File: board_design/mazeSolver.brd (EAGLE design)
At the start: 130 x 130 mm, 53 parts, among them IC1 L293DD, IC2 7805TV, IC3 CP2101, Q1 BC547, Q2 BC547, U1 MPU-9250, U2 AP1509-SOP8L, U3 ESP-WROOM-32, U4 GY-521MPU6050

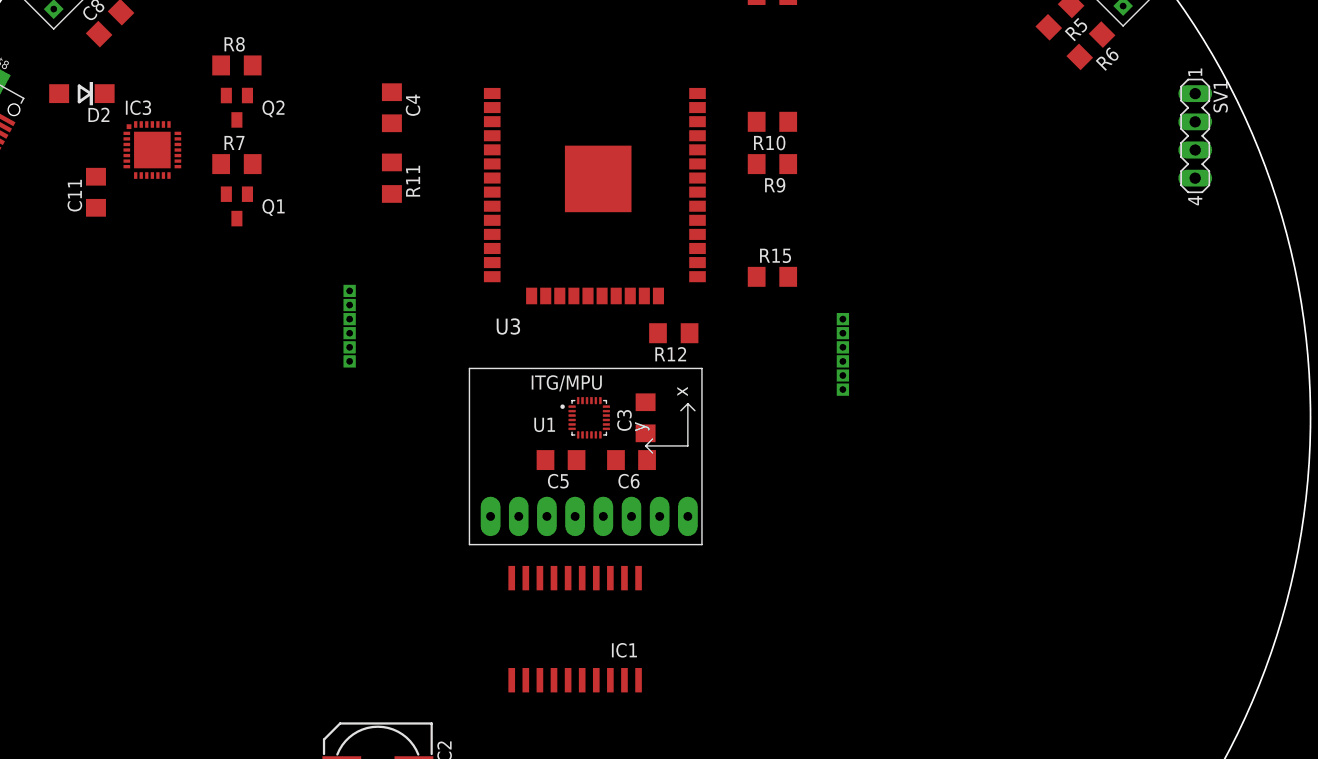
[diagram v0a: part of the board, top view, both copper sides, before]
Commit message: Components placement
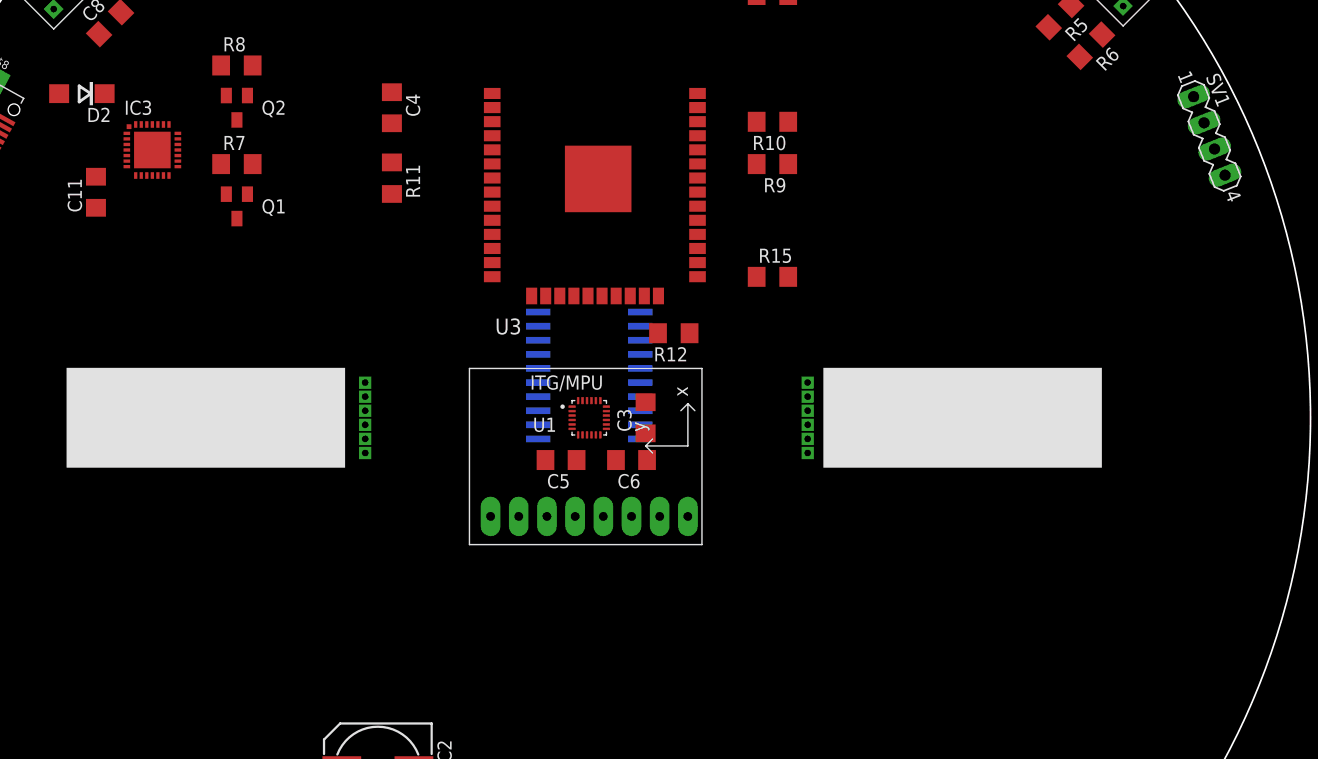
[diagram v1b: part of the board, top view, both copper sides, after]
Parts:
- moved IC1 22.9 mm to (0.00, 3.81), flipped to the bottom, turned to 270 degrees
- moved U$3 14.7 mm to (-20.2, -3.17), turned to 90 degrees
- moved U$2 6.54 mm to (19.7, 3.17)
- moved SV1 1.27 mm to (55.9, 25.4), turned to 291.8 degrees

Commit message: Routing
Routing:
- net +3V3: track 0.00 -> 543.4 mm, vias 0 -> 6
- net VCC: track 0.00 -> 171.8 mm, vias 0 -> 1
- net TXD: track 0.00 -> 109.8 mm, vias 0 -> 2
- net RXD: track 0.00 -> 101.4 mm, vias 0 -> 2
- net IO0: track 0.00 -> 100.5 mm, vias 0 -> 4
- net SCL: track 0.00 -> 92.7 mm, vias 0 -> 2
- net SDA: track 0.00 -> 91.2 mm
- net EN: track 0.00 -> 65.8 mm
- net INT: track 0.00 -> 65.1 mm, vias 0 -> 1
- net N$4: track 0.00 -> 61.2 mm
- net RTS: track 0.00 -> 55.2 mm, vias 0 -> 2
- net CTS: track 0.00 -> 54.7 mm, vias 0 -> 2
- net N$5: track 0.00 -> 53.3 mm
- net ENCA2: track 0.00 -> 51.0 mm, vias 0 -> 3
- net N$2: track 0.00 -> 50.2 mm, vias 0 -> 1
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- added copper zone on layer 1, net GND
- added copper zone on layer 16, net GND

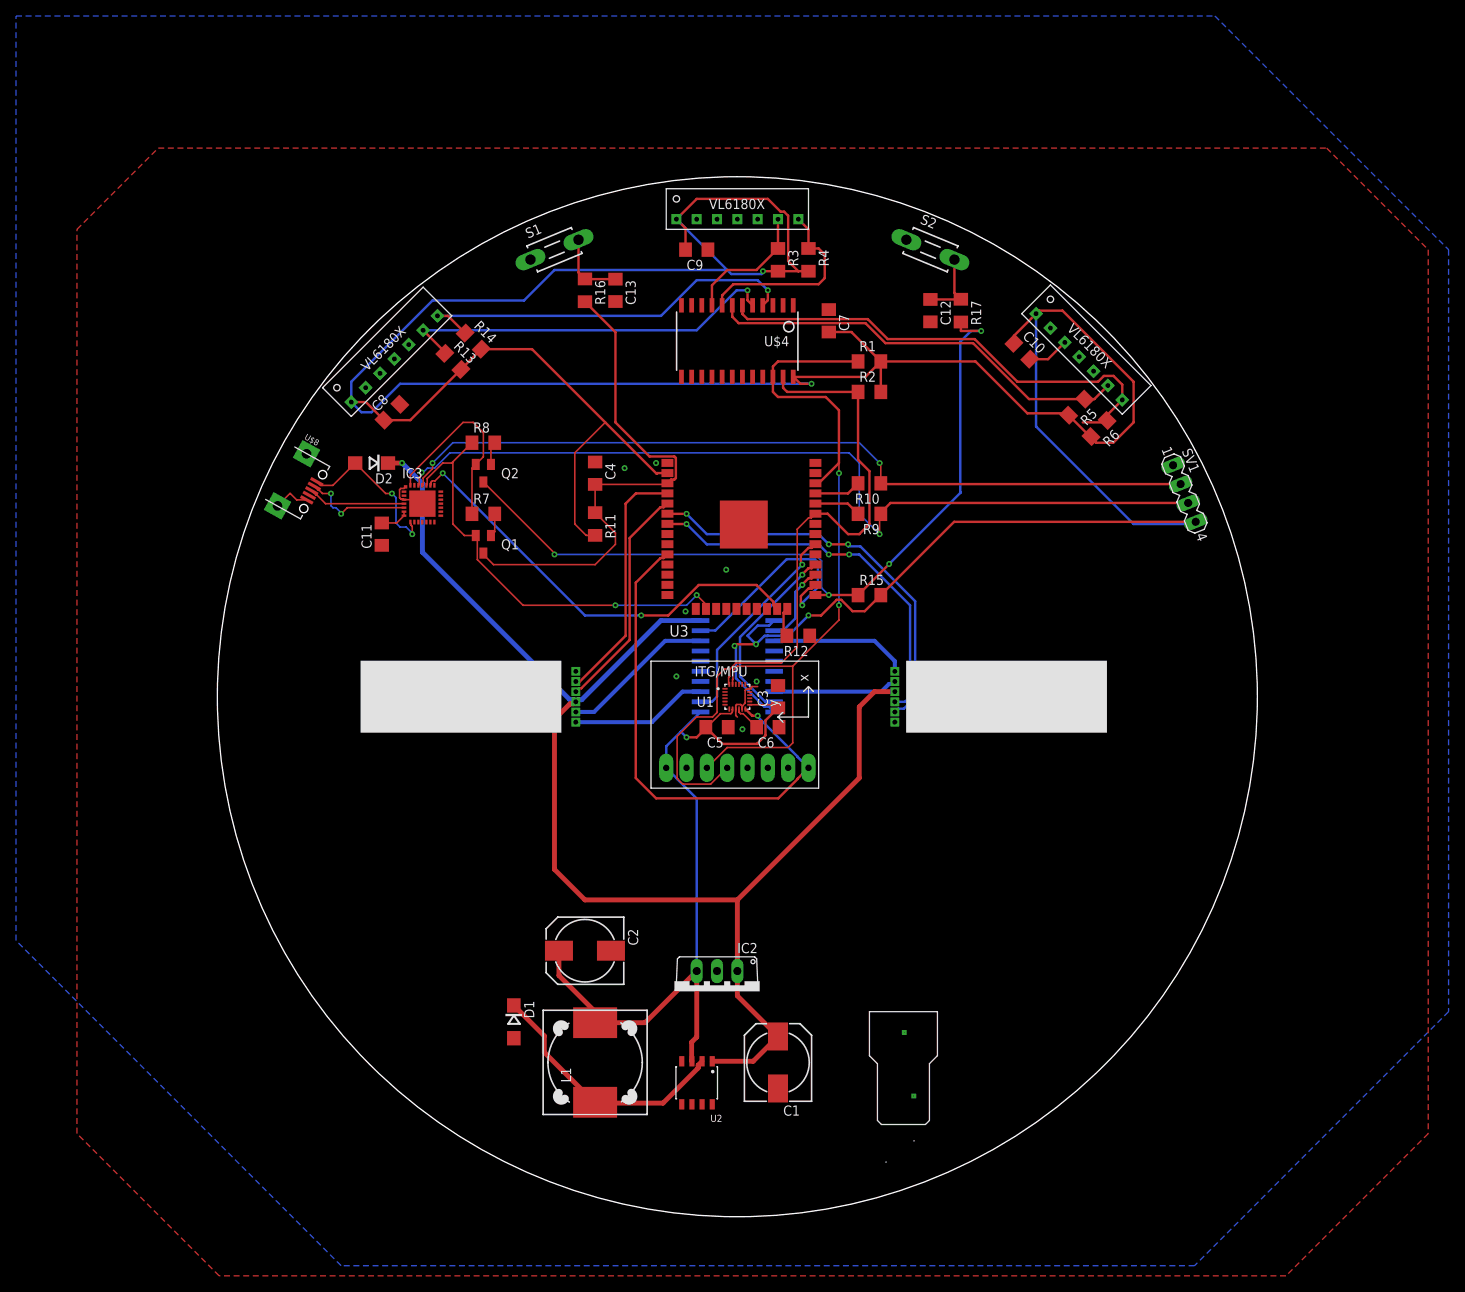
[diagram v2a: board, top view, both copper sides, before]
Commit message: Added mounting holes
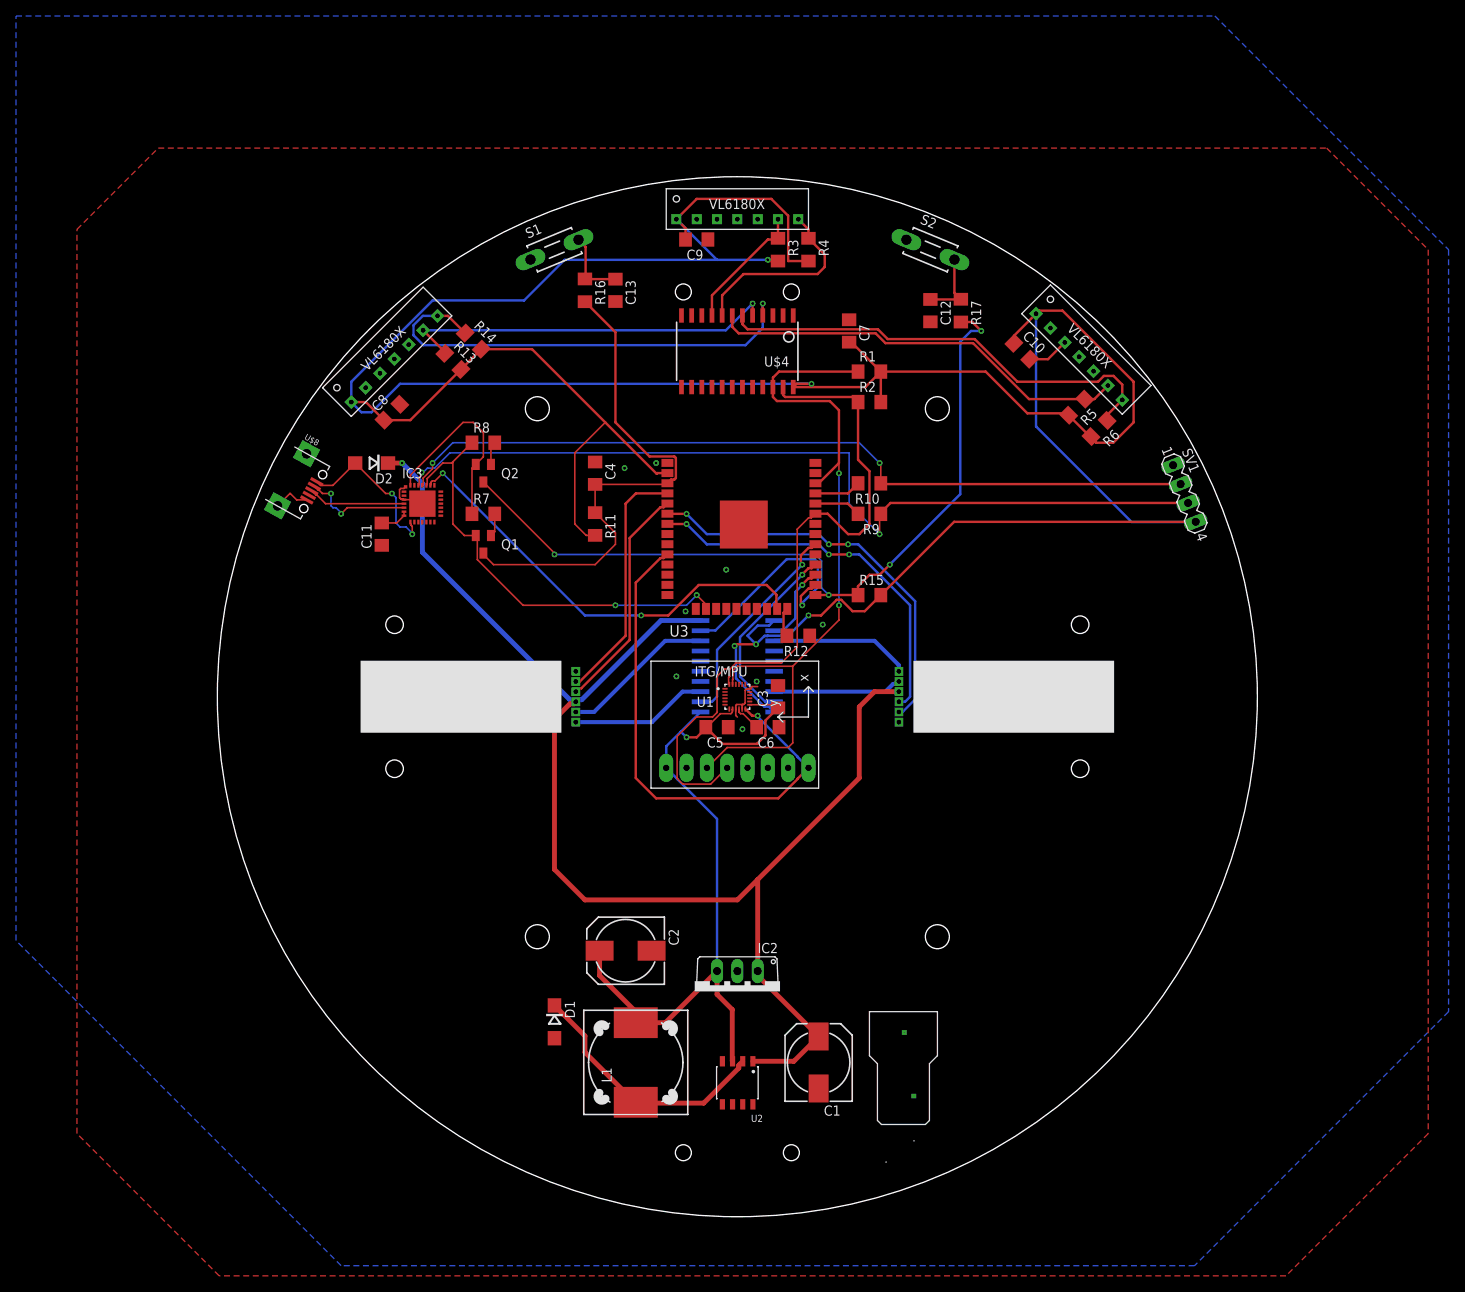
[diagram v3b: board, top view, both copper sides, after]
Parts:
- moved D1 5.08 mm to (-22.9, -40.6)
- moved L1 5.08 mm to (-12.7, -45.7)
- moved C1 5.08 mm to (10.2, -45.7)
- moved C2 5.08 mm to (-14.0, -31.8)
- moved U2 5.08 mm to (0.00, -48.3)
- moved C7 2.84 mm to (14.0, 45.7)
- moved IC2 2.54 mm to (0.00, -36.8)
- moved R2 1.27 mm to (16.5, 36.8)
- moved R3 1.27 mm to (5.08, 55.9)
- moved R4 1.27 mm to (8.89, 55.9)
- moved U$4 1.27 mm to (0.00, 43.2)
- moved C9 1.27 mm to (-5.08, 57.1)
- moved R1 1.27 mm to (16.5, 40.6)
- moved U$2 0.51 mm to (20.2, 3.17)
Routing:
- net +3V3: track 543.4 -> 533.5 mm
- net N$2: track 50.2 -> 58.7 mm
- net VCC: track 171.8 -> 175.9 mm
- net N$4: track 61.2 -> 57.9 mm
- net SDA: track 91.2 -> 89.7 mm
- net SCL: track 92.7 -> 91.8 mm
- net CTS: track 54.7 -> 55.5 mm
- net N$1: track 48.8 -> 48.1 mm
- net N$5: track 53.3 -> 52.8 mm
- net OUTA2: track 15.6 -> 16.1 mm
- net ENCA1: track 48.1 -> 47.6 mm
- net ENCA2: track 51.0 -> 50.5 mm
- net GND: track 21.8 -> 21.7 mm, vias 7 -> 8

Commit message: PCB Design
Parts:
- removed S1: RST, switch-tact:DTS-3
- removed S2: BOOT, switch-tact:DTS-3
- added U5: RST, Switches:SW4_236X236H5MM
- added U6: BOOT, Switches:SW4_236X236H5MM
- moved R3 2.84 mm to (2.54, 57.1), turned to 180 degrees
- moved R4 1.80 mm to (10.2, 57.1), turned to 0 degrees
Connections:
- net GND: now also U$1.P$2, U5.1, U5.2, U6.1, U6.2; no longer S1.1, S2.1, U$1.P-2
- net N$14: now also U5.3, U5.4; no longer S1.2
- net N$15: now also U6.3, U6.4; no longer S2.2
- net VCC: now also U$1.P$1; no longer U$1.P-1
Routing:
- net GND: track 21.7 -> 59.8 mm, vias 8 -> 9
- net +3V3: track 533.5 -> 519.9 mm, vias 6 -> 5
- net VCC: track 175.9 -> 187.5 mm
- net N$15: track 9.11 -> 16.1 mm
- net N$6: track 24.1 -> 19.1 mm
- net N$14: track 9.12 -> 13.1 mm
- net N$4: track 57.9 -> 61.2 mm
- net N$7: track 16.1 -> 15.4 mm
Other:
- outline, holes or cut-outs redrawn
